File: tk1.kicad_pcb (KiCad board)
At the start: 2 copper layers, 84.9 x 53.8 mm, 70 parts, among them P1 USB_C_Plug, U1 MCP1824T-2502EOT, U10 PT2043AT6, U2 MIC5258-1.2YM5, U3 CH552E, U5 USBLC6-2SC6, U6 ICE40UP5K-SG48ITR, U8 W25Q80DVUXIE, U9 NCP752BSN33T1G

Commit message: V2
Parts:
- removed C27: 1pF, Capacitor_SMD:C_0805_2012Metric
- removed C8: 1uF, Capacitor_SMD:C_0805_2012Metric
- removed R30: 2k, Resistor_SMD:R_0805_2012Metric
- removed U10: PT2043AT6, Package_TO_SOT_SMD:SOT-23-6
- D1: footprint LED_SMD:LED_0402_1005Metric -> LED_SMD:LED_0805_2012Metric
- U8: value W25Q80DVUXIE -> SOIC-8; footprint mta1:W25Q80DVUXIE -> Package_SO:SOIC-8_3.9x4.9mm_P1.27mm
- moved TP15 5.08 mm to (121.9, 54.4)
- moved TP28 4.11 mm to (152.0, 99.0)
- moved C1 3.56 mm to (127.5, 49.2)
- moved R1 3.56 mm to (118.9, 49.2)
- moved FID1 2.96 mm to (104.0, 47.0)
- moved TP3 2.61 mm to (134.0, 93.0)
- moved TP13 2.59 mm to (136.1, 53.3)
- moved C18 2.56 mm to (133.4, 72.8), turned to 45 degrees
- moved C6 2.03 mm to (120.4, 64.6)
- moved R3 1.95 mm to (135.8, 70.2)
- moved FID2 1.83 mm to (172.2, 90.4)
- moved C19 1.44 mm to (154.3, 51.0)
- moved TP18 1.14 mm to (148.8, 79.2)
- moved D1 1.02 mm to (132.0, 68.6)
- moved C26 0.51 mm to (146.4, 57.4)
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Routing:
- net GND: track 709.4 -> 647.6 mm
- net +1V2: track 194.2 -> 217.7 mm
- net /Application FPGA/TOUCH_PAD: track 20.2 -> 0.00 mm
- net TOUCH_EVENT: track 14.6 -> 0.00 mm
- net +3.3V: track 276.6 -> 289.7 mm
- net +2V5: track 54.6 -> 64.7 mm
- net Net-(U10-TCH): track 9.36 -> 0.00 mm
- net +5V: track 154.8 -> 162.7 mm
- net SPI_VCC_OK: track 42.5 -> 38.5 mm
- net Net-(U2-EN): track 7.96 -> 11.5 mm
- net APP_ICE_MOSI: track 57.5 -> 59.2 mm
- net /Application FPGA/APP_FLASH_HOLD: track 11.3 -> 12.9 mm
- net APP_ICE_SS: track 48.0 -> 46.3 mm
- net APP_ICE_MISO: track 79.9 -> 81.4 mm
- net /Application FPGA/APP_FLASH_WP: track 17.9 -> 19.4 mm
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- removed copper zone on F.Cu, net /Application FPGA/TOUCH_PAD
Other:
- board size 84.9 x 53.8 mm -> 83 x 58 mm

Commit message: V3
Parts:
- moved TP16 41.0 mm to (174.3, 89.6)
- moved R20 34.0 mm to (173.9, 85.8)
- moved TP21 10.3 mm to (155.0, 72.5)
- moved TP17 8.02 mm to (153.9, 58.6)
- moved R18 6.26 mm to (167.7, 84.1)
- moved TP5 5.45 mm to (112.4, 57.7)
- moved R19 3.91 mm to (139.5, 65.6), turned to -45 degrees
- moved TP12 3.73 mm to (146.2, 60.2)
- moved FID2 3.66 mm to (168.6, 91.0)
- moved R24 2.52 mm to (131.4, 56.4), turned to 90 degrees
- moved C5 2.24 mm to (131.9, 50.5)
- moved TP20 2.03 mm to (154.5, 76.6)
- moved U2 1.67 mm to (120.6, 57.7), turned to 180 degrees
- moved R1 1.22 mm to (118.8, 50.4)
- moved U3 1.05 mm to (121.4, 82.6)
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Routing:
- net APP_CRESET: track 27.4 -> 295.8 mm, vias 0 -> 2
- net VCC_OK: track 28.5 -> 278.2 mm, vias 0 -> 2
- net +3.3V: track 289.7 -> 454.4 mm, vias 3 -> 4
- net TOUCH_EVENT: track 0.00 -> 38.1 mm, vias 0 -> 2
- net GND: track 647.6 -> 672.9 mm, vias 8 -> 9
- net APP_ICE_MISO: track 81.4 -> 60.6 mm
- net +1V2: track 217.7 -> 235.5 mm, vias 0 -> 2
- net APP_CDONE: track 13.6 -> 25.1 mm
- net APP_ICE_SCK: track 31.7 -> 42.8 mm, vias 0 -> 4
- net APP_GPIO4: track 16.2 -> 5.20 mm
- net Net-(D3-BK): track 16.2 -> 8.59 mm
- net SPI_VCC_OK: track 38.5 -> 31.0 mm, vias 0 -> 2
- net Net-(U2-EN): track 11.5 -> 7.20 mm
- net /Application FPGA/APP_FLASH_HOLD: track 12.9 -> 8.70 mm
- net APP_LED_BLUE: track 23.3 -> 20.8 mm
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- added copper zone on F.Cu, net TOUCH_EVENT

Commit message: V4
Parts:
- removed D3: LED_ARGB, mta1:0402rgb-1010
- removed P1: USB_C_Plug, mta1:U261-241N-4BS60
- removed R29: 5.1k, Resistor_SMD:R_0805_2012Metric
- added REF**: LED_0805_2012Metric_Pad1.15x1.40mm_HandSolder, LED_SMD:LED_0805_2012Metric_Pad1.15x1.40mm_HandSolder, F.Cu at (166.3, 86.9)
- added REF**: LED_0805_2012Metric_Pad1.15x1.40mm_HandSolder, LED_SMD:LED_0805_2012Metric_Pad1.15x1.40mm_HandSolder, F.Cu at (166.3, 84.5)
- added REF**: LED_0805_2012Metric_Pad1.15x1.40mm_HandSolder, LED_SMD:LED_0805_2012Metric_Pad1.15x1.40mm_HandSolder, F.Cu at (166.3, 89.3)
- added REF**: USB_A_Kycon_KUSBX-AS1N-B_Horizontal, Connector_USB:USB_A_Kycon_KUSBX-AS1N-B_Horizontal, F.Cu at (101.5, 78.7)
- moved U5 4.53 mm to (116.7, 74.4)
- moved R18 4.17 mm to (164.7, 81.2)
- moved FID2 1.21 mm to (167.5, 91.5)
- moved C13 0.95 mm to (116.8, 79.2)
- moved C2 0.65 mm to (123.3, 95.0)
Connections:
- U6 pad 4: unconnected-(U6-IOB_8a-Pad4) -> TOUCH_EVENT
- U6 pad 6: TOUCH_EVENT -> (no net)
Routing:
- net GND: track 672.9 -> 635.1 mm
- net TOUCH_EVENT: track 38.1 -> 17.7 mm, vias 2 -> 0
- net +5V: track 162.3 -> 143.4 mm
- net VCC_OK: track 278.2 -> 267.1 mm
- net /USB to Serial converter/INT_USB_IN_D-: track 15.0 -> 21.7 mm
- net Net-(P1-CC): track 6.46 -> 0.00 mm
- net Net-(D3-BK): track 8.59 -> 2.67 mm
- net +3.3V: track 454.4 -> 459.4 mm
- net APP_LED_BLUE: track 20.8 -> 16.6 mm
- net INT_USB_D+: track 16.5 -> 20.7 mm
- net INT_USB_D-: track 13.3 -> 17.3 mm
- net /USB to Serial converter/INT_USB_IN_D+: track 12.0 -> 15.8 mm
- net Net-(D3-GK): track 8.96 -> 5.68 mm
- net +1V2: track 235.5 -> 234.6 mm
- net APP_CRESET: track 295.8 -> 295.3 mm
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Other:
- outline, holes or cut-outs redrawn

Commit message: V5
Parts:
- removed the REF** at (166.3, 86.9)
- removed the REF** at (166.3, 84.5)
- removed the REF** at (166.3, 89.3)
- removed the REF** at (101.5, 78.7)
- added D2: LEDred, LED_SMD:LED_0805_2012Metric_Pad1.15x1.40mm_HandSolder, F.Cu at (166.3, 84.6)
- added D3: LEDgreen, LED_SMD:LED_0805_2012Metric_Pad1.15x1.40mm_HandSolder, F.Cu at (166.3, 87.0)
- added D4: LEDblue, LED_SMD:LED_0805_2012Metric_Pad1.15x1.40mm_HandSolder, F.Cu at (166.3, 89.5)
- added J1: USB_A, Connector_USB:USB_A_Kycon_KUSBX-AS1N-B_Horizontal, F.Cu at (101.5, 78.8)
- moved TP5 15.4 mm to (127.5, 54.5)
- moved TP15 5.97 mm to (127.0, 57.5)
- moved TP21 2.24 mm to (157.0, 73.5)
- moved C13 1.84 mm to (118.5, 80.0)
- turned C3 to 90 degrees
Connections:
- U6 pad 4: TOUCH_EVENT -> unconnected-(U6-IOB_8a-Pad4)
- U6 pad 6: (no net) -> TOUCH_EVENT
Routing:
- net GND: track 635.1 -> 609.5 mm
- net unconnected-(U6-IOB_8a-Pad4): track 0.00 -> 17.7 mm
- net TOUCH_EVENT: track 17.7 -> 0.00 mm
- net +5V: track 143.4 -> 137.7 mm, vias 1 -> 0
- net APP_ICE_MISO: track 60.4 -> 54.8 mm
- net INT_USB_D-: track 17.3 -> 13.9 mm
- net +3.3V: track 459.4 -> 462.3 mm
- net VCC_OK: track 267.1 -> 265.8 mm
- net +1V2: track 234.6 -> 235.4 mm
- net APP_GPIO4: track 5.20 -> 5.96 mm
- net SPI_VCC_OK: track 30.8 -> 30.1 mm

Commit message: V6
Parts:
- added R4: 10k, Resistor_SMD:R_0805_2012Metric, F.Cu at (159.5, 53.3)
- added SW1: SW_Push, Button_Switch_THT:SW_PUSH_6mm, F.Cu at (163.5, 53.4)
- moved C16 7.86 mm to (161.7, 66.0)
- moved D4 5.00 mm to (166.3, 84.5)
- moved D2 4.70 mm to (166.3, 89.3)
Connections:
- D2 pad 1: Net-(D4-K) -> Net-(D2-K)
- D4 pad 1: Net-(D2-K) -> Net-(D4-K)
- U6 pad 4: unconnected-(U6-IOB_8a-Pad4) -> (no net)
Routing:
- net TOUCH_EVENT: track 0.00 -> 43.3 mm
- net +3.3V: track 462.3 -> 489.5 mm
- net unconnected-(U6-IOB_8a-Pad4): track 17.7 -> 0.00 mm
- net GND: track 609.5 -> 615.8 mm
- net +1V2: track 235.4 -> 241.1 mm
- removed copper zone on F.Cu, net TOUCH_EVENT

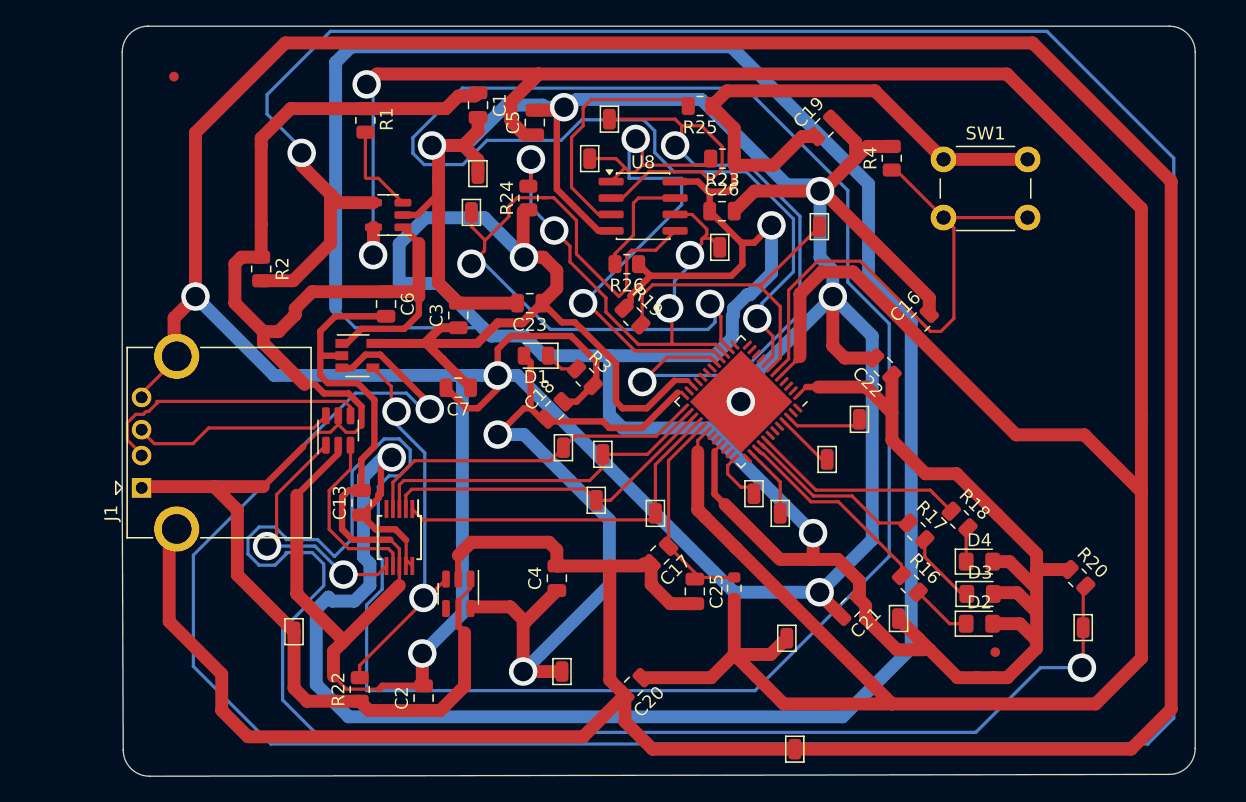
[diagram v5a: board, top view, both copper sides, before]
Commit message: Correction condensateur en trop + PCB correspondant au schéma
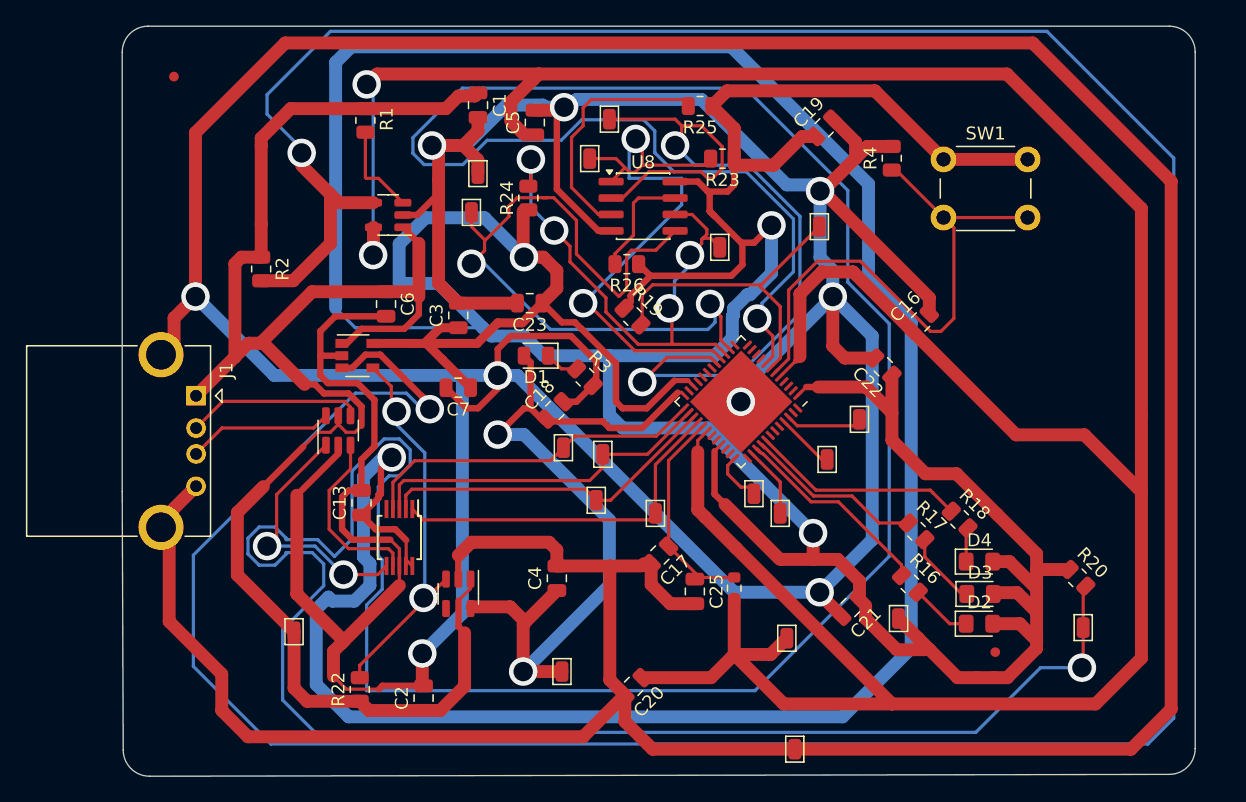
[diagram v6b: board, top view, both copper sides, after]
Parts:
- removed C26: 0.10uF, Capacitor_SMD:C_0805_2012Metric
- removed REF**: logo, mta1:logo_OPENHARDWARE_4mmX4mm
- moved J1 8.28 mm to (105.7, 71.7), turned to -90 degrees
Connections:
- U6 pad 4: (no net) -> unconnected-(U6-IOB_8a-Pad4)
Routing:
- net /USB to Serial converter/INT_USB_IN_D-: track 21.8 -> 13.6 mm
- net GND: track 615.8 -> 609.0 mm
- net /USB to Serial converter/INT_USB_IN_D+: track 15.8 -> 11.3 mm
- net +5V: track 137.7 -> 135.3 mm
- net +3.3V: track 489.5 -> 490.3 mm

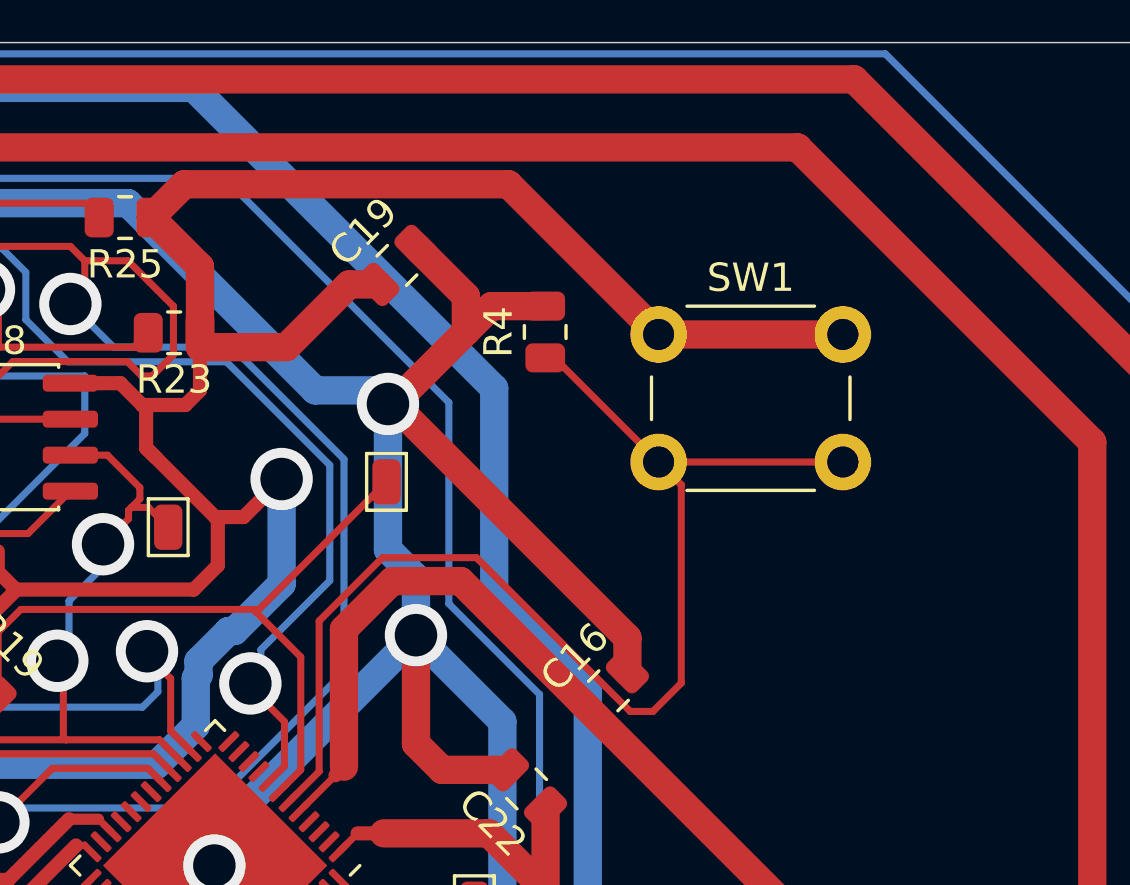
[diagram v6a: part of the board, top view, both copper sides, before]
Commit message: Ajout bouton du même style que les projets du LabCyber
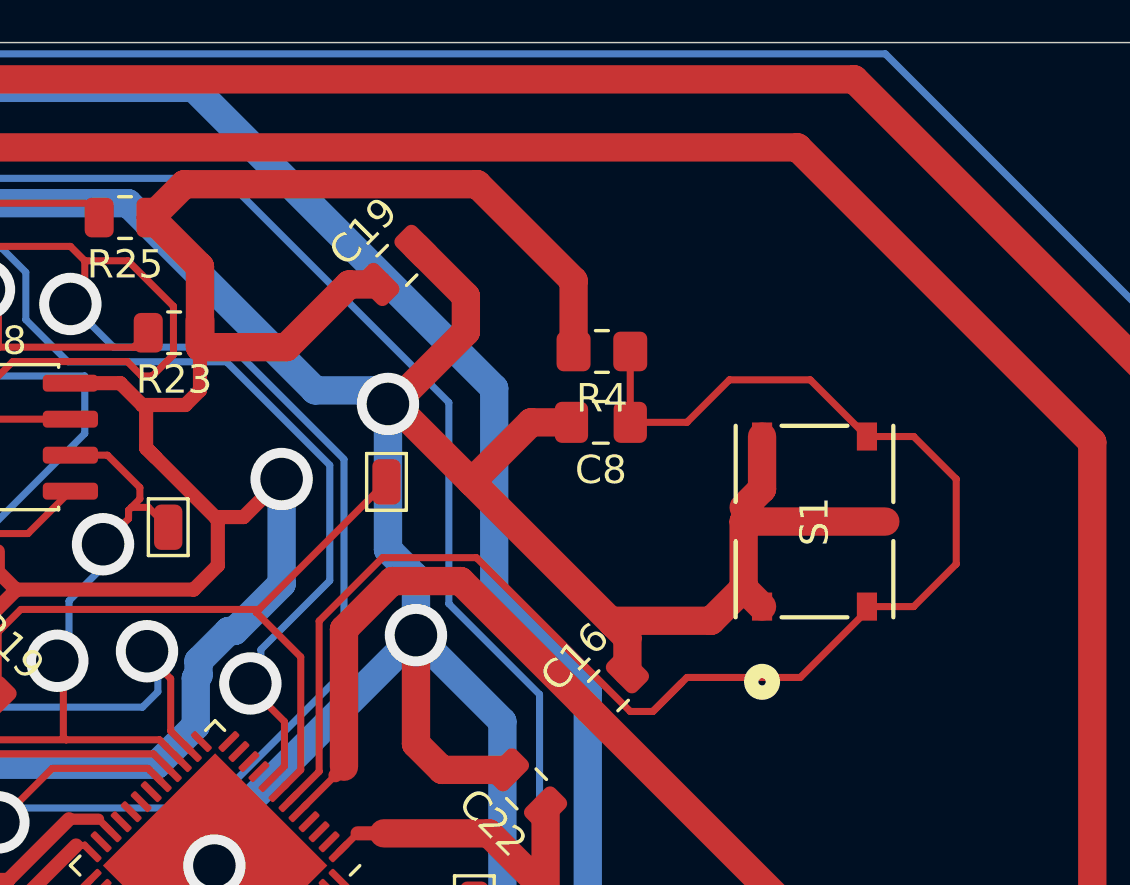
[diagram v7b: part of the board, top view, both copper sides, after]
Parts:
- removed SW1: SW_Push, Button_Switch_THT:SW_PUSH_6mm
- added C8: 1u, Capacitor_SMD:C_0805_2012Metric_Pad1.18x1.45mm_HandSolder, F.Cu at (161.5, 56.5)
- added S1: PTS526_SMG15J_SMTR2_LFS, MyFootprints:PTS526SMG15JSMTR2LFS, F.Cu at (169.0, 60.0)
- R4: value 10k -> 10K; footprint Resistor_SMD:R_0805_2012Metric -> Resistor_SMD:R_0805_2012Metric_Pad1.20x1.40mm_HandSolder
- moved R4 2.11 mm to (161.5, 54.0), turned to 180 degrees
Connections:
- net TOUCH_EVENT renamed /Application FPGA/Button/NO
- R4 pad 2: GND -> +3.3V
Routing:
- net GND: track 609.0 -> 627.0 mm
- net /Application FPGA/Button/NO: track 43.3 -> 55.2 mm
- net +3.3V: track 490.3 -> 482.5 mm
